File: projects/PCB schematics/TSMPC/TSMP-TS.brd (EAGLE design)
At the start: 81.3 x 70 mm, 23 parts, among them J1 2P_1-770166-0, J2 2P_1-770166-0, J3 2P_1-770166-0

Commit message: TEMP - Initial board placement.
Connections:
- new net HV+_POST_AIR+: J1.1, J1.2
- net HV+: no longer J1.1, J1.2
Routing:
- net HV+: track 13.7 -> 0.14 mm
- net HV+_POST_AIR+: track 0.00 -> 4.14 mm
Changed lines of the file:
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@@
 <signal name="HV+">
 <contactref element="R1" pad="1"/>
-<contactref element="J1" pad="2"/>
-<contactref element="J1" pad="1"/>
-<wire x1="22.225" y1="64.77" x2="18.0848" y2="64.77" width="1.27" layer="1"/>
-<wire x1="18.0848" y1="64.77" x2="18.1102" y2="55.3406" width="1.27" layer="1"/>
 <wire x1="18.1102" y1="55.3406" x2="18.2058" y2="55.245" width="0.8128" layer="1"/>
 </signal>
@@
 <wire x1="23.8058" y1="55.245" x2="27.045" y2="55.245" width="1.27" layer="1"/>
 </signal>
+<signal name="HV+_POST_AIR+">
+<contactref element="J1" pad="2"/>
+<contactref element="J1" pad="1"/>
+<wire x1="22.225" y1="64.77" x2="18.0848" y2="64.77" width="1.27" layer="1"/>
+</signal>
 </signals>

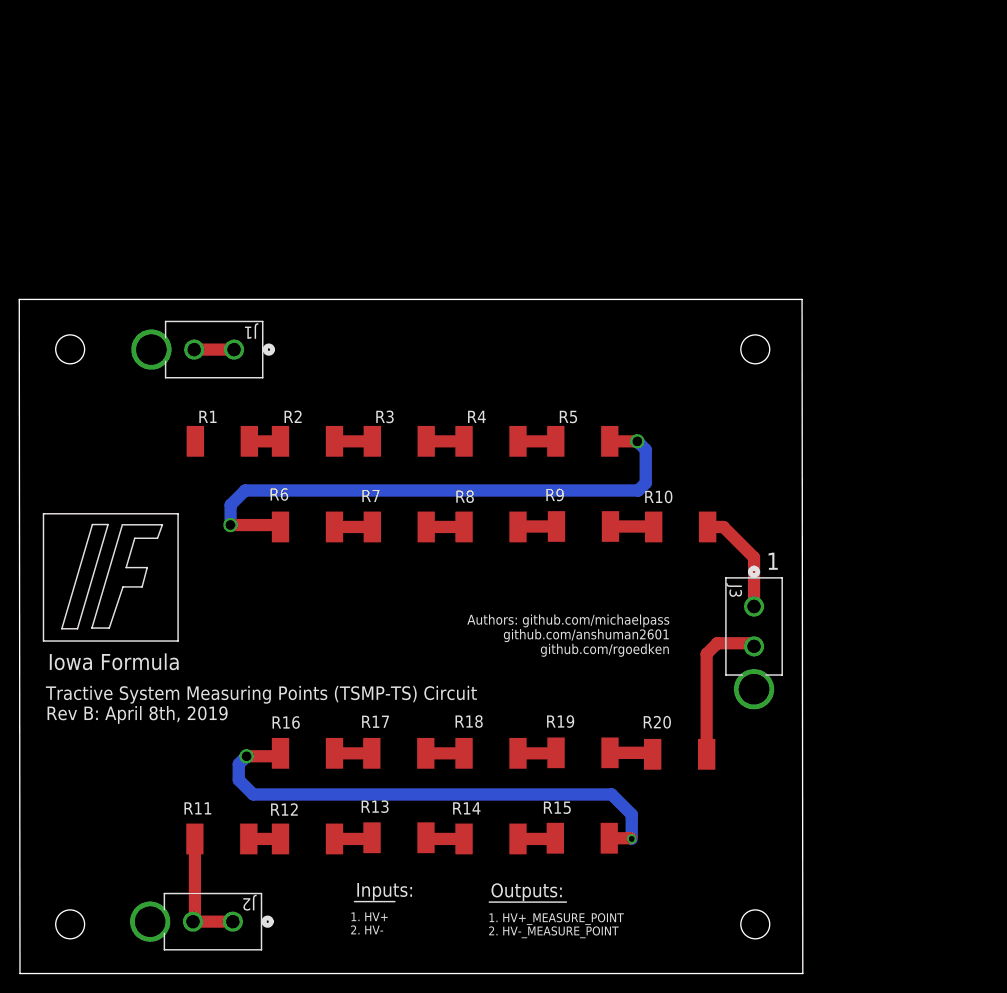
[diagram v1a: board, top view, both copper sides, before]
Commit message: TSMPC - Board 3900milx3900mil redo.
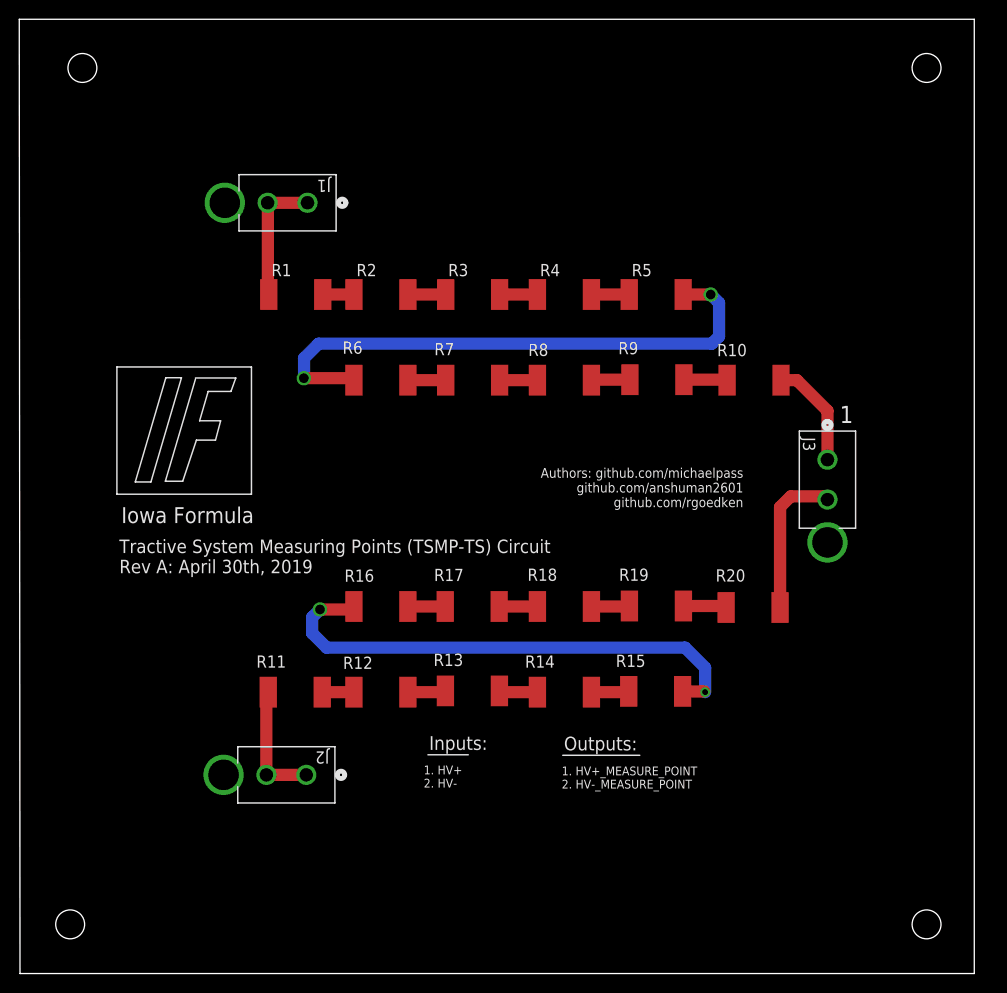
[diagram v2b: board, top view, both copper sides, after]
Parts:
- moved J1 17.0 mm to (29.8, 80.0)
- moved R1 17.0 mm to (28.6, 70.5)
- moved R10 17.0 mm to (76.2, 61.6)
- moved R12 17.0 mm to (37.5, 29.2)
- moved R16 17.0 mm to (37.5, 38.1)
- moved R2 17.0 mm to (37.5, 70.5)
- moved R3 17.0 mm to (47.0, 70.5)
- moved R5 17.0 mm to (66.0, 70.5)
- moved R6 17.0 mm to (37.5, 61.6)
- moved R7 17.0 mm to (47.0, 61.6)
- moved R9 17.0 mm to (66.1, 61.6)
- moved J2 17.0 mm to (29.7, 20.6)
- moved R11 17.0 mm to (28.6, 29.2)
- moved R17 17.0 mm to (46.9, 38.1)
- moved R18 17.0 mm to (56.5, 38.1)
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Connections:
- net HV- renamed HV-_POST_AIR-
- removed net HV+: R1.1
- net HV+_POST_AIR+: now also R1.1
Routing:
- net HV+_POST_AIR+: track 4.14 -> 13.7 mm
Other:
- board size 81.3 x 70 mm -> 99.1 x 99.1 mm
- board text added: "Tractive System Measuring Points (TSMP-TS) Circuit Rev A: April 30th, 2019"
- board text removed: "Tractive System Measuring Points (TSMP-TS) Circuit Rev B: April 8th, 2019"

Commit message: PROJ - Final pre-purchase revisions (4 boards still in progress.)
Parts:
- renumbered J1 to HV+_POST_AIR+, J2 to HV-_POST_AIR-, J3 to HV_MEASURE
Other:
- board text added: "HV_MEASURE: 1. HV+_MEASURE_POINT 2. HV-_MEASURE_POINT"
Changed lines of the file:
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@@
             github.com/rgoedken
              </text>
-<hole x="6.477" y="94.0054" drill="3"/>
+<hole x="5.207" y="94.0054" drill="3"/>
 <hole x="94.107" y="94.0054" drill="3"/>
 <hole x="5.207" y="5.1054" drill="3"/>
@@
 <wire x1="56.3372" y1="22.6568" x2="64.3382" y2="22.6568" width="0.1524" layer="25"/>
 <text x="85.09" y="57.15" size="1.778" layer="25">1</text>
+<text x="81.28" y="36.83" size="1.016" layer="25">HV_MEASURE:
+1. HV+_MEASURE_POINT
+2. HV-_MEASURE_POINT</text>
 </plain>
 <attributes>
@@
 <attribute name="NAME" x="24.5364" y="31.75" size="1.27" layer="25"/>
 </element>
-<element name="J1" library="con-MATE-N-LOK" package="CON2_1X2_P163_VMNL-1MTG" value="2P_1-770166-0" x="29.845" y="80.01" smashed="yes" rot="R180">
+<element name="HV+_POST_AIR+" library="con-MATE-N-LOK" package="CON2_1X2_P163_VMNL-1MTG" value="2P_1-770166-0" x="29.845" y="80.01" smashed="yes" rot="R180">
 <attribute name="MANUFACTURER_PART_NUMBER" value="17701660" x="29.845" y="80.01" size="1.778" layer="27" rot="R180" display="off"/>
-<attribute name="NAME" x="32.2834" y="82.3976" size="1.27" layer="25" ratio="6" rot="SR180"/>
+<attribute name="NAME" x="18.5166" y="83.9724" size="1.27" layer="25" ratio="6" rot="SR0"/>
 <attribute name="VENDOR" value="TE Connectivity" x="29.845" y="80.01" size="1.778" layer="27" rot="R180" display="off"/>
 </element>
-<element name="J2" library="con-MATE-N-LOK" package="CON2_1X2_P163_VMNL-1MTG" value="2P_1-770166-0" x="29.718" y="20.6248" smashed="yes" rot="R180">
+<element name="HV-_POST_AIR-" library="con-MATE-N-LOK" package="CON2_1X2_P163_VMNL-1MTG" value="2P_1-770166-0" x="29.718" y="20.6248" smashed="yes" rot="R180">
 <attribute name="MANUFACTURER_PART_NUMBER" value="17701660" x="29.718" y="20.6248" size="1.778" layer="27" rot="R180" display="off"/>
-<attribute name="NAME" x="32.1056" y="23.0632" size="1.27" layer="25" ratio="6" rot="SR180"/>
+<attribute name="NAME" x="18.6944" y="15.0368" size="1.27" layer="25" ratio="6" rot="SR0"/>
 <attribute name="VENDOR" value="TE Connectivity" x="29.718" y="20.6248" size="1.778" layer="27" rot="R180" display="off"/>
 </element>
-<element name="J3" library="con-MATE-N-LOK" package="CON2_1X2_P163_VMNL-1MTG" value="2P_1-770166-0" x="83.82" y="53.34" smashed="yes" rot="R270">
+<element name="HV_MEASURE" library="con-MATE-N-LOK" package="CON2_1X2_P163_VMNL-1MTG" value="2P_1-770166-0" x="83.82" y="53.34" smashed="yes" rot="R270">
 <attribute name="MANUFACTURER_PART_NUMBER" value="17701660" x="83.82" y="53.34" size="1.778" layer="27" rot="R270" display="off"/>
-<attribute name="NAME" x="81.28" y="55.6768" size="1.27" layer="25" ratio="6" rot="SR270"/>
+<attribute name="NAME" x="88.9" y="44.6532" size="1.27" layer="25" ratio="6" rot="SR90"/>
 <attribute name="VENDOR" value="TE Connectivity" x="83.82" y="53.34" size="1.778" layer="27" rot="R270" display="off"/>
 </element>
@@
 <signal name="HV+_MEASURE_POINT">
 <contactref element="R10" pad="2"/>
-<contactref element="J3" pad="1"/>
+<contactref element="HV_MEASURE" pad="1"/>
 <wire x1="79" y1="61.595" x2="80.645" y2="61.595" width="1.27" layer="1"/>
 <wire x1="80.645" y1="61.595" x2="83.82" y2="58.42" width="1.27" layer="1"/>
@@
 <signal name="HV-_MEASURE_POINT">
 <contactref element="R20" pad="2"/>
-<contactref element="J3" pad="2"/>
+<contactref element="HV_MEASURE" pad="2"/>
 <wire x1="83.4898" y1="49.53" x2="80.01" y2="49.53" width="1.27" layer="1"/>
 <wire x1="83.4898" y1="49.53" x2="83.82" y2="49.1998" width="1.27" layer="1"/>
@@
 </signal>
 <signal name="HV+_POST_AIR+">
-<contactref element="J1" pad="2"/>
-<contactref element="J1" pad="1"/>
+<contactref element="HV+_POST_AIR+" pad="2"/>
+<contactref element="HV+_POST_AIR+" pad="1"/>
 <wire x1="29.845" y1="80.01" x2="25.7048" y2="80.01" width="1.27" layer="1"/>
 <contactref element="R1" pad="1"/>
@@
 </signal>
 <signal name="HV-_POST_AIR-">
-<contactref element="J2" pad="2"/>
-<contactref element="J2" pad="1"/>
+<contactref element="HV-_POST_AIR-" pad="2"/>
+<contactref element="HV-_POST_AIR-" pad="1"/>
 <contactref element="R11" pad="1"/>
 <wire x1="25.5778" y1="20.6248" x2="29.718" y2="20.6248" width="1.27" layer="1"/>

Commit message: PROJ - Gerber files major milestone - 05/05/19.
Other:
- board text added: "Tractive System Measuring Points (TSMP-TS) Circuit Rev A: May 5th, 2019"
- board text removed: "Tractive System Measuring Points (TSMP-TS) Circuit Rev A: April 30th, 2019"
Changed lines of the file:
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@@
 <text x="10.5156" y="46.7614" size="1.651" layer="25" font="vector">Iowa Formula</text>
 <text x="10.3124" y="41.5544" size="1.397" layer="25" font="vector">Tractive System Measuring Points (TSMP-TS) Circuit
-Rev A: April 30th, 2019</text>
+Rev A: May 5th, 2019</text>
 <text x="75.0824" y="52.4764" size="1.016" layer="25" font="vector" rot="R180">Authors: github.com/michaelpass
             github.com/anshuman2601
